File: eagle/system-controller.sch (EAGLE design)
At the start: 234 parts, among them CN1 22u, IC1 TS4100, J1 1, Q0 MOSFET-P-N-PAIR, Q1 MOSFET-P-N-PAIR, Q10 DNP/NTR4101P, Q11 DNP/NTR4101P, Q12 DNP/NTR4101P, Q13 DON3035L, Q2 MOSFET-P-N-PAIR, Q3 MOSFET-P-N-PAIR, Q4 MOSFET-P-N-PAIR, Q5 MOSFET-P-N-PAIR, Q6 MOSFET-P-N-PAIR, Q7 MOSFET-P-N-PAIR, Q9 DNP/NTR4101P, SW0 TPS25944LRVCRWQFN-20-3X4, SW1 TPS25944LRVCRWQFN-20-3X4, SW2 TPS25944LRVCRWQFN-20-3X4, SW3 TPS25944LRVCRWQFN-20-3X4, SW4 TPS25944LRVCRWQFN-20-3X4, SW5 TPS25944LRVCRWQFN-20-3X4, SW6 TPS25944LRVCRWQFN-20-3X4, SW7 TPS25944LRVCRWQFN-20-3X4, U1 MEGA128-A, X1 8 MHz CRYSTAL-ABRACON-ABM3-SMD

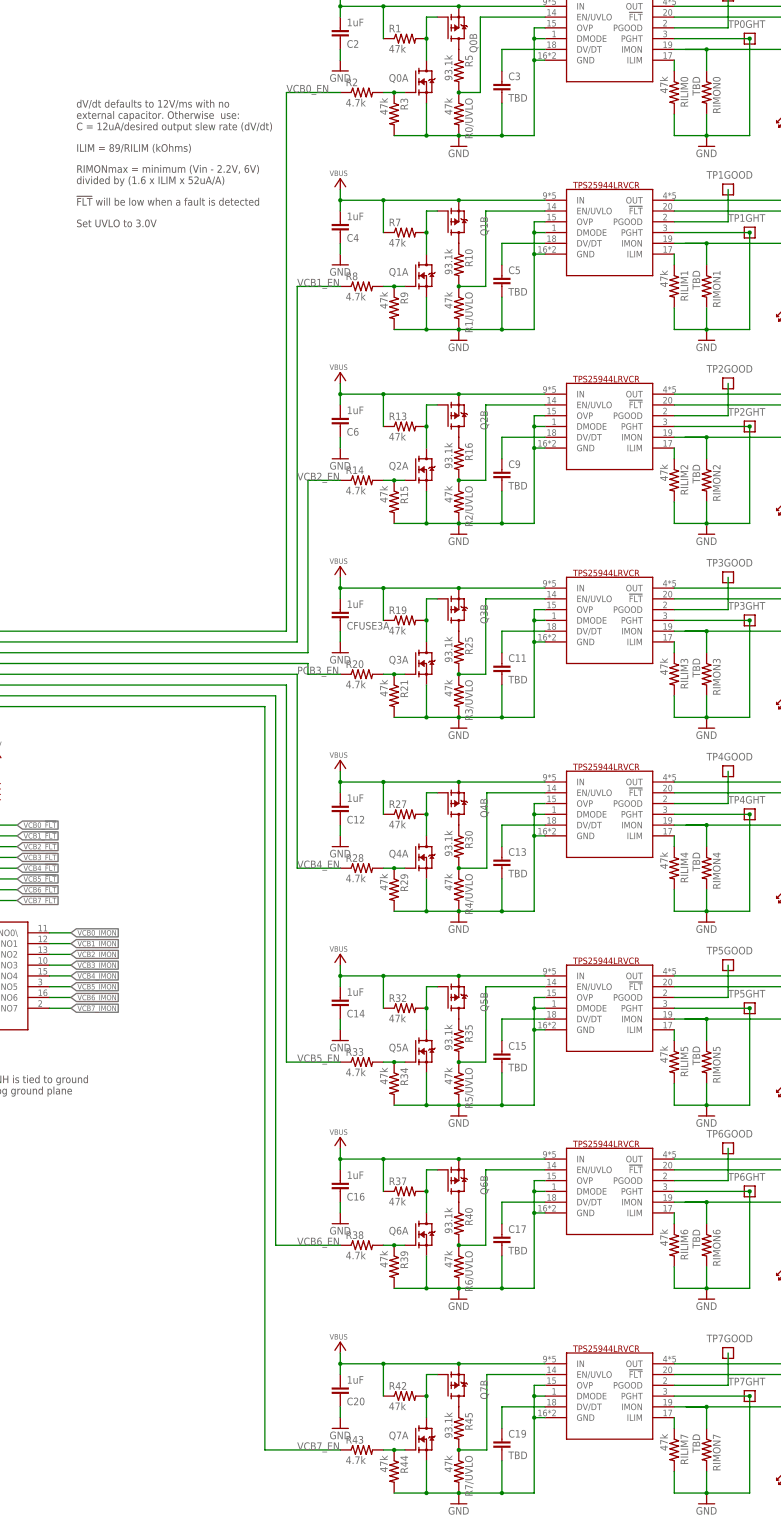
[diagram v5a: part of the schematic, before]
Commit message: added the RIMON resister value and dV/dt cap value
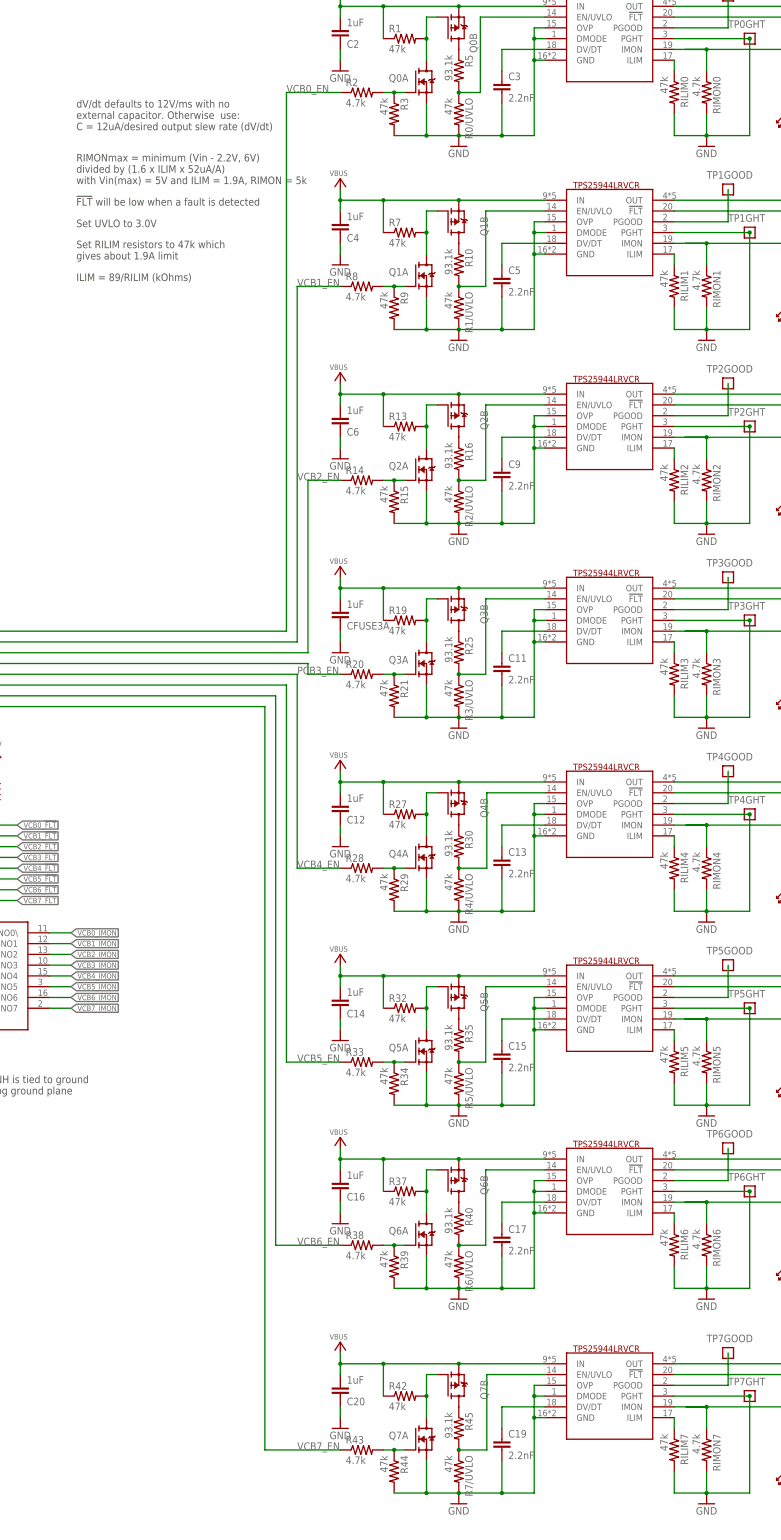
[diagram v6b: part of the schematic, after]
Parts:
- C11, C13, C15, C17, C19, C3, C5, C9: value TBD -> 2.2nF
- RIMON0, RIMON1, RIMON2, RIMON3, RIMON4, RIMON5, RIMON6, RIMON7: value TBD -> 4.7k
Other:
- note added: "RIMONmax = minimum (Vin - 2.2V, 6V) divided by (1.6 x ILIM x 52uA/A) with Vin(max) = 5V and ILIM = 1.9A, RIMON = 5k"
- note added: "Set RILIM resistors to 47k which gives about 1.9A limit"
- note added: "To Do: Look at RIMON equations"
- note removed: "RIMONmax = minimum (Vin - 2.2V, 6V) divided by (1.6 x ILIM x 52uA/A)"
- note removed: "To Do List: -Determine resistor values for voltage divider -Determine RC values for time constant"
- note removed: "Todo: Determine ILIM for each switch Set RILIM resistors to 47k which gives about 1.9A limit"
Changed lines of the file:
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@@
 <attribute name="MPN" value="Texas Instruments"/>
 </part>
-<part name="RIMON0" library="rcl_custom" deviceset="R-US_" device="0603-B-NOSILK" value="TBD"/>
+<part name="RIMON0" library="rcl_custom" deviceset="R-US_" device="0603-B-NOSILK" value="4.7k"/>
 <part name="GND" library="psas_c3_team05" deviceset="GND" device=""/>
-<part name="C3" library="rcl_custom" deviceset="C-EU" device="0603-B-NOSILK" value="TBD"/>
+<part name="C3" library="rcl_custom" deviceset="C-EU" device="0603-B-NOSILK" value="2.2nF"/>
 <part name="R4" library="rcl_custom" deviceset="R-US_" device="0603-B-NOSILK" value="390">
 <attribute name="DIST" value="digikey"/>
@@
 <part name="GND5" library="psas_c3_team05" deviceset="GND" device=""/>
 <part name="SW1" library="WQFN-20-3x4" deviceset="TPS25944LRVCR" device="WQFN-20-3X4"/>
-<part name="RIMON1" library="rcl_custom" deviceset="R-US_" device="0603-B-NOSILK" value="TBD"/>
+<part name="RIMON1" library="rcl_custom" deviceset="R-US_" device="0603-B-NOSILK" value="4.7k"/>
 <part name="GND19" library="psas_c3_team05" deviceset="GND" device=""/>
-<part name="C5" library="rcl_custom" deviceset="C-EU" device="0603-B-NOSILK" value="TBD"/>
+<part name="C5" library="rcl_custom" deviceset="C-EU" device="0603-B-NOSILK" value="2.2nF"/>
 <part name="GND20" library="psas_c3_team05" deviceset="GND" device=""/>
 <part name="VOP2" library="oresat-eagle" deviceset="VBUS" device=""/>
@@
 <part name="3V-11" library="supply-3v" deviceset="3V" device=""/>
 <part name="SW2" library="WQFN-20-3x4" deviceset="TPS25944LRVCR" device="WQFN-20-3X4"/>
-<part name="RIMON2" library="rcl_custom" deviceset="R-US_" device="0603-B-NOSILK" value="TBD"/>
+<part name="RIMON2" library="rcl_custom" deviceset="R-US_" device="0603-B-NOSILK" value="4.7k"/>
 <part name="GND27" library="psas_c3_team05" deviceset="GND" device=""/>
-<part name="C9" library="rcl_custom" deviceset="C-EU" device="0603-B-NOSILK" value="TBD"/>
+<part name="C9" library="rcl_custom" deviceset="C-EU" device="0603-B-NOSILK" value="2.2nF"/>
 <part name="GND28" library="psas_c3_team05" deviceset="GND" device=""/>
 <part name="VOP3" library="oresat-eagle" deviceset="VBUS" device=""/>
@@
 <part name="GND30" library="psas_c3_team05" deviceset="GND" device=""/>
 <part name="SW7" library="WQFN-20-3x4" deviceset="TPS25944LRVCR" device="WQFN-20-3X4"/>
-<part name="RIMON7" library="rcl_custom" deviceset="R-US_" device="0603-B-NOSILK" value="TBD"/>
+<part name="RIMON7" library="rcl_custom" deviceset="R-US_" device="0603-B-NOSILK" value="4.7k"/>
 <part name="GND31" library="psas_c3_team05" deviceset="GND" device=""/>
-<part name="C19" library="rcl_custom" deviceset="C-EU" device="0603-B-NOSILK" value="TBD"/>
+<part name="C19" library="rcl_custom" deviceset="C-EU" device="0603-B-NOSILK" value="2.2nF"/>
 <part name="GND32" library="psas_c3_team05" deviceset="GND" device=""/>
 <part name="VOP4" library="oresat-eagle" deviceset="VBUS" device=""/>
@@
 <part name="GND34" library="psas_c3_team05" deviceset="GND" device=""/>
 <part name="SW5" library="WQFN-20-3x4" deviceset="TPS25944LRVCR" device="WQFN-20-3X4"/>
-<part name="RIMON5" library="rcl_custom" deviceset="R-US_" device="0603-B-NOSILK" value="TBD"/>
+<part name="RIMON5" library="rcl_custom" deviceset="R-US_" device="0603-B-NOSILK" value="4.7k"/>
 <part name="GND36" library="psas_c3_team05" deviceset="GND" device=""/>
-<part name="C15" library="rcl_custom" deviceset="C-EU" device="0603-B-NOSILK" value="TBD"/>
+<part name="C15" library="rcl_custom" deviceset="C-EU" device="0603-B-NOSILK" value="2.2nF"/>
 <part name="GND37" library="psas_c3_team05" deviceset="GND" device=""/>
 <part name="VOP5" library="oresat-eagle" deviceset="VBUS" device=""/>
@@
 <part name="GND39" library="psas_c3_team05" deviceset="GND" device=""/>
 <part name="SW4" library="WQFN-20-3x4" deviceset="TPS25944LRVCR" device="WQFN-20-3X4"/>
-<part name="RIMON4" library="rcl_custom" deviceset="R-US_" device="0603-B-NOSILK" value="TBD"/>
+<part name="RIMON4" library="rcl_custom" deviceset="R-US_" device="0603-B-NOSILK" value="4.7k"/>
 <part name="GND40" library="psas_c3_team05" deviceset="GND" device=""/>
-<part name="C13" library="rcl_custom" deviceset="C-EU" device="0603-B-NOSILK" value="TBD"/>
+<part name="C13" library="rcl_custom" deviceset="C-EU" device="0603-B-NOSILK" value="2.2nF"/>
 <part name="GND41" library="psas_c3_team05" deviceset="GND" device=""/>
 <part name="VOP6" library="oresat-eagle" deviceset="VBUS" device=""/>
@@
 <part name="GND43" library="psas_c3_team05" deviceset="GND" device=""/>
 <part name="SW3" library="WQFN-20-3x4" deviceset="TPS25944LRVCR" device="WQFN-20-3X4"/>
-<part name="RIMON3" library="rcl_custom" deviceset="R-US_" device="0603-B-NOSILK" value="TBD"/>
+<part name="RIMON3" library="rcl_custom" deviceset="R-US_" device="0603-B-NOSILK" value="4.7k"/>
 <part name="GND44" library="psas_c3_team05" deviceset="GND" device=""/>
-<part name="C11" library="rcl_custom" deviceset="C-EU" device="0603-B-NOSILK" value="TBD"/>
+<part name="C11" library="rcl_custom" deviceset="C-EU" device="0603-B-NOSILK" value="2.2nF"/>
 <part name="GND45" library="psas_c3_team05" deviceset="GND" device=""/>
 <part name="VOP7" library="oresat-eagle" deviceset="VBUS" device=""/>
@@
 <part name="GND47" library="psas_c3_team05" deviceset="GND" device=""/>
 <part name="SW6" library="WQFN-20-3x4" deviceset="TPS25944LRVCR" device="WQFN-20-3X4"/>
-<part name="RIMON6" library="rcl_custom" deviceset="R-US_" device="0603-B-NOSILK" value="TBD"/>
+<part name="RIMON6" library="rcl_custom" deviceset="R-US_" device="0603-B-NOSILK" value="4.7k"/>
 <part name="GND48" library="psas_c3_team05" deviceset="GND" device=""/>
-<part name="C17" library="rcl_custom" deviceset="C-EU" device="0603-B-NOSILK" value="TBD"/>
+<part name="C17" library="rcl_custom" deviceset="C-EU" device="0603-B-NOSILK" value="2.2nF"/>
 <part name="GND49" library="psas_c3_team05" deviceset="GND" device=""/>
 <part name="VOP8" library="oresat-eagle" deviceset="VBUS" device=""/>
@@
 <plain>
 <text x="455.93" y="30.48" size="2.54" layer="97">William Harrington, James Heath, Shan Quinney</text>
-<text x="60.96" y="328.93" size="1.778" layer="99">To Do List:
--Determine resistor values for voltage divider
--Determine RC values for time constant</text>
 <wire x1="129.54" y1="406.4" x2="205.74" y2="406.4" width="0.1524" layer="97" style="longdash"/>
 <wire x1="205.74" y1="406.4" x2="205.74" y2="360.68" width="0.1524" layer="97" style="longdash"/>
@@
 6. IMU
 7. SDR-GPS</text>
-<text x="308.61" y="351.79" size="1.778" layer="99">Todo:
-Determine ILIM for each switch
+<text x="308.61" y="356.87" size="1.778" layer="97">
 Set RILIM resistors to 47k which
 gives about 1.9A limit</text>
@@
 C = 12uA/desired output slew rate (dV/dt)</text>
 <text x="308.61" y="374.65" size="1.778" layer="97">RIMONmax = minimum (Vin - 2.2V, 6V)
-divided by (1.6 x ILIM x 52uA/A)</text>
-<text x="308.61" y="382.27" size="1.778" layer="97">ILIM = 89/RILIM (kOhms)</text>
+divided by (1.6 x ILIM x 52uA/A)
+with Vin(max) = 5V and ILIM = 1.9A, RIMON = 5k</text>
+<text x="308.61" y="351.79" size="1.778" layer="97">ILIM = 89/RILIM (kOhms)</text>
 <text x="308.61" y="369.57" size="1.778" layer="97">!FLT! will be low when a fault is detected</text>
 <text x="308.61" y="364.49" size="1.778" layer="97">Set UVLO to 3.0V</text>
@@
 V_TH max = 1.4V</text>
 <text x="233.68" y="132.08" size="1.778" layer="97">P-Channel MOSFET</text>
+<text x="307.34" y="345.44" size="1.778" layer="99">To Do: Look at RIMON equations</text>
 </plain>
 <instances>

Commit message: latest minor changes
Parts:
- RIMON0, RIMON1, RIMON2, RIMON3, RIMON4, RIMON5, RIMON6, RIMON7: value 4.7k -> 47k
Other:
- note added: "To Do: Look at RIMON equations Polarity chech (phoroisolator)"
- note removed: "To Do: Look at RIMON equations"
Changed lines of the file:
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@@
 <attribute name="MPN" value="Texas Instruments"/>
 </part>
-<part name="RIMON0" library="rcl_custom" deviceset="R-US_" device="0603-B-NOSILK" value="4.7k"/>
+<part name="RIMON0" library="rcl_custom" deviceset="R-US_" device="0603-B-NOSILK" value="47k"/>
 <part name="GND" library="psas_c3_team05" deviceset="GND" device=""/>
 <part name="C3" library="rcl_custom" deviceset="C-EU" device="0603-B-NOSILK" value="2.2nF"/>
@@
 <part name="GND5" library="psas_c3_team05" deviceset="GND" device=""/>
 <part name="SW1" library="WQFN-20-3x4" deviceset="TPS25944LRVCR" device="WQFN-20-3X4"/>
-<part name="RIMON1" library="rcl_custom" deviceset="R-US_" device="0603-B-NOSILK" value="4.7k"/>
+<part name="RIMON1" library="rcl_custom" deviceset="R-US_" device="0603-B-NOSILK" value="47k"/>
 <part name="GND19" library="psas_c3_team05" deviceset="GND" device=""/>
 <part name="C5" library="rcl_custom" deviceset="C-EU" device="0603-B-NOSILK" value="2.2nF"/>
@@
 <part name="3V-11" library="supply-3v" deviceset="3V" device=""/>
 <part name="SW2" library="WQFN-20-3x4" deviceset="TPS25944LRVCR" device="WQFN-20-3X4"/>
-<part name="RIMON2" library="rcl_custom" deviceset="R-US_" device="0603-B-NOSILK" value="4.7k"/>
+<part name="RIMON2" library="rcl_custom" deviceset="R-US_" device="0603-B-NOSILK" value="47k"/>
 <part name="GND27" library="psas_c3_team05" deviceset="GND" device=""/>
 <part name="C9" library="rcl_custom" deviceset="C-EU" device="0603-B-NOSILK" value="2.2nF"/>
@@
 <part name="GND30" library="psas_c3_team05" deviceset="GND" device=""/>
 <part name="SW7" library="WQFN-20-3x4" deviceset="TPS25944LRVCR" device="WQFN-20-3X4"/>
-<part name="RIMON7" library="rcl_custom" deviceset="R-US_" device="0603-B-NOSILK" value="4.7k"/>
+<part name="RIMON7" library="rcl_custom" deviceset="R-US_" device="0603-B-NOSILK" value="47k"/>
 <part name="GND31" library="psas_c3_team05" deviceset="GND" device=""/>
 <part name="C19" library="rcl_custom" deviceset="C-EU" device="0603-B-NOSILK" value="2.2nF"/>
@@
 <part name="GND34" library="psas_c3_team05" deviceset="GND" device=""/>
 <part name="SW5" library="WQFN-20-3x4" deviceset="TPS25944LRVCR" device="WQFN-20-3X4"/>
-<part name="RIMON5" library="rcl_custom" deviceset="R-US_" device="0603-B-NOSILK" value="4.7k"/>
+<part name="RIMON5" library="rcl_custom" deviceset="R-US_" device="0603-B-NOSILK" value="47k"/>
 <part name="GND36" library="psas_c3_team05" deviceset="GND" device=""/>
 <part name="C15" library="rcl_custom" deviceset="C-EU" device="0603-B-NOSILK" value="2.2nF"/>
@@
 <part name="GND39" library="psas_c3_team05" deviceset="GND" device=""/>
 <part name="SW4" library="WQFN-20-3x4" deviceset="TPS25944LRVCR" device="WQFN-20-3X4"/>
-<part name="RIMON4" library="rcl_custom" deviceset="R-US_" device="0603-B-NOSILK" value="4.7k"/>
+<part name="RIMON4" library="rcl_custom" deviceset="R-US_" device="0603-B-NOSILK" value="47k"/>
 <part name="GND40" library="psas_c3_team05" deviceset="GND" device=""/>
 <part name="C13" library="rcl_custom" deviceset="C-EU" device="0603-B-NOSILK" value="2.2nF"/>
@@
 <part name="GND43" library="psas_c3_team05" deviceset="GND" device=""/>
 <part name="SW3" library="WQFN-20-3x4" deviceset="TPS25944LRVCR" device="WQFN-20-3X4"/>
-<part name="RIMON3" library="rcl_custom" deviceset="R-US_" device="0603-B-NOSILK" value="4.7k"/>
+<part name="RIMON3" library="rcl_custom" deviceset="R-US_" device="0603-B-NOSILK" value="47k"/>
 <part name="GND44" library="psas_c3_team05" deviceset="GND" device=""/>
 <part name="C11" library="rcl_custom" deviceset="C-EU" device="0603-B-NOSILK" value="2.2nF"/>
@@
 <part name="GND47" library="psas_c3_team05" deviceset="GND" device=""/>
 <part name="SW6" library="WQFN-20-3x4" deviceset="TPS25944LRVCR" device="WQFN-20-3X4"/>
-<part name="RIMON6" library="rcl_custom" deviceset="R-US_" device="0603-B-NOSILK" value="4.7k"/>
+<part name="RIMON6" library="rcl_custom" deviceset="R-US_" device="0603-B-NOSILK" value="47k"/>
 <part name="GND48" library="psas_c3_team05" deviceset="GND" device=""/>
 <part name="C17" library="rcl_custom" deviceset="C-EU" device="0603-B-NOSILK" value="2.2nF"/>
@@
 V_TH max = 1.4V</text>
 <text x="233.68" y="132.08" size="1.778" layer="97">P-Channel MOSFET</text>
-<text x="307.34" y="345.44" size="1.778" layer="99">To Do: Look at RIMON equations</text>
+<text x="265.176" y="309.88" size="1.778" layer="99">To Do: Look at RIMON equations
+Polarity chech (phoroisolator)</text>
 </plain>
 <instances>
